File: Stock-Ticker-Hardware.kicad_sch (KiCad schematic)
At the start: 0 parts

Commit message: Start schematic
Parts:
- added A1: RaspberryPi_Pico_W, Module:RaspberryPi_Pico_W_SMD_HandSolder, symbol MCU_Module:RaspberryPi_Pico_W_Debug
- added J1: Conn_01x05_Socket, Connector_JST:JST_XH_B5B-XH-A_1x05_P2.50mm_Vertical, symbol Connector:Conn_01x05_Socket
- added SW1: SW_Push, Button_Switch_THT:SW_PUSH-12mm, symbol Switch:SW_Push
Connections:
- new net: A1.22 (GPIO17), SW1.1
- new net +5V: A1.40 (VBUS), J1.5 (Pin_5)
- new net CLK: A1.4 (GPIO2), J1.1 (Pin_1)
- new net CS: A1.5 (GPIO3), J1.3 (Pin_3)
- new net DOUT: A1.7 (GPIO5), J1.2 (Pin_2)
- new net GND: A1.13 (GND), A1.18 (GND), A1.23 (GND), A1.28 (GND), A1.3 (GND), A1.38 (GND), A1.8 (GND), A1.D2 (GND), J1.4 (Pin_4), SW1.2

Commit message: Finish basic schematic
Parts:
- added H1, H2, H3, H4: MountingHole, MountingHole:MountingHole_2.7mm_M2.5, symbol Mechanical:MountingHole
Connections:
- no-connect marks 0 -> 30
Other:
- title: (none) -> Stock Ticker Hardware
- moved on the sheet: A1, J1, SW1

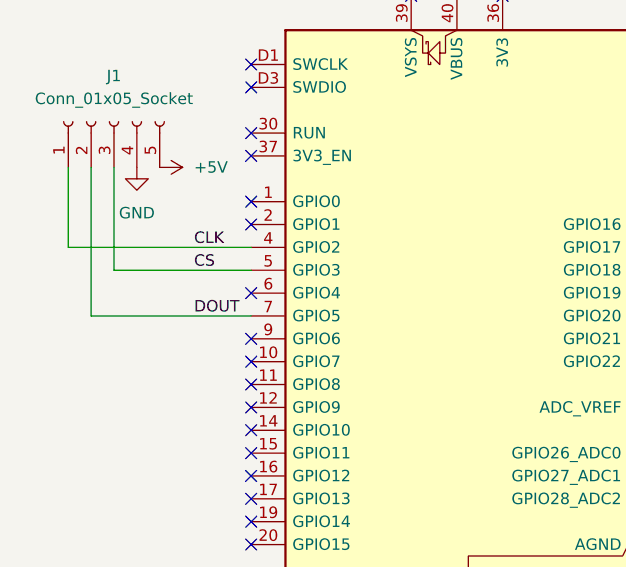
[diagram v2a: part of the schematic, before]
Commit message: Correct wiring from Pico to JST XH
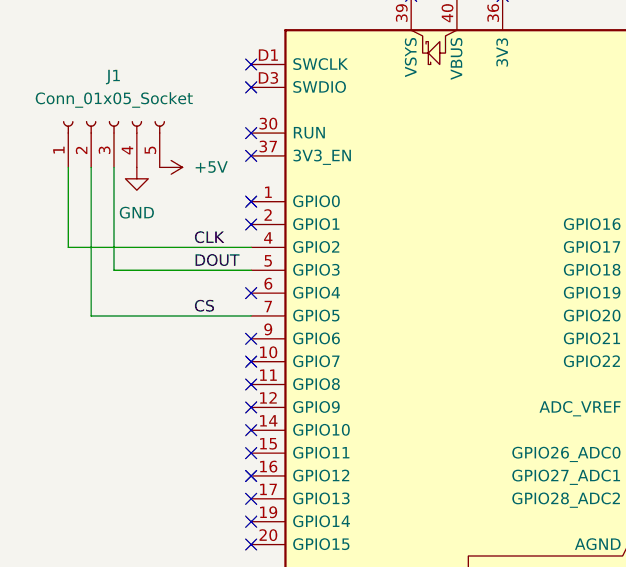
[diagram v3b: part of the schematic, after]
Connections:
- net CS: now also A1.7 (GPIO5), J1.2 (Pin_2); no longer A1.5 (GPIO3), J1.3 (Pin_3)
- net DOUT: now also A1.5 (GPIO3), J1.3 (Pin_3); no longer A1.7 (GPIO5), J1.2 (Pin_2)
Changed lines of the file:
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@@
+	(wire
+		(pts
+			(xy 99.06 90.17) (xy 114.3 90.17)
+		)
+		(stroke
+			(width 0)
+			(type default)
+		)
+	)
 	(wire
 		(pts
 			(xy 99.06 78.74) (xy 99.06 90.17)
+		)
+		(stroke
+			(width 0)
+			(type default)
+		)
+	)
+	(wire
+		(pts
+			(xy 96.52 95.25) (xy 114.3 95.25)
 		)
 		(stroke
@@
 		)
 	)
-	(wire
-		(pts
-			(xy 99.06 90.17) (xy 114.3 90.17)
-		)
-		(stroke
-			(width 0)
-			(type default)
-		)
-	)
-	(wire
-		(pts
-			(xy 96.52 95.25) (xy 114.3 95.25)
-		)
-		(stroke
-			(width 0)
-			(type default)
-		)
-	)
 	(label "CLK"
 		(at 107.95 87.63 0)
@@
 	)
 	(label "CS"
-		(at 107.95 90.17 0)
+		(at 107.95 95.25 0)
 		(effects
 			(font
@@
 	)
 	(label "DOUT"
-		(at 107.95 95.25 0)
+		(at 107.95 90.17 0)
 		(effects
 			(font

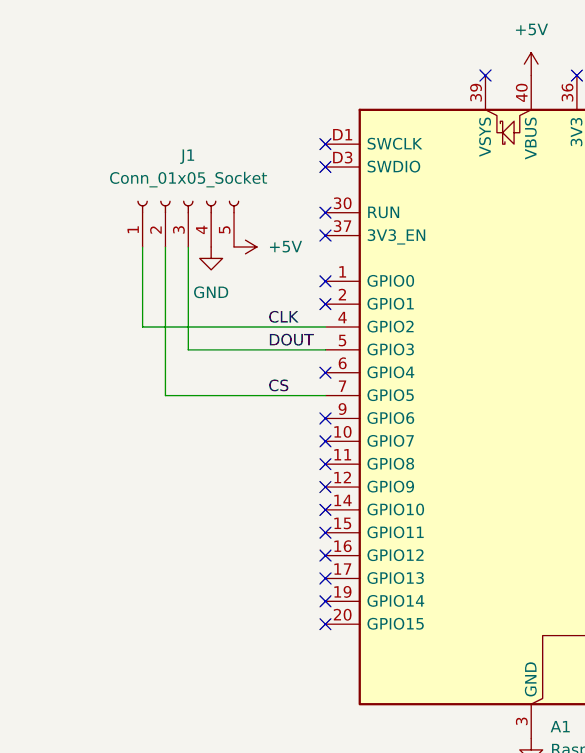
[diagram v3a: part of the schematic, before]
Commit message: Add connectors for SWD and UART for easy debugging
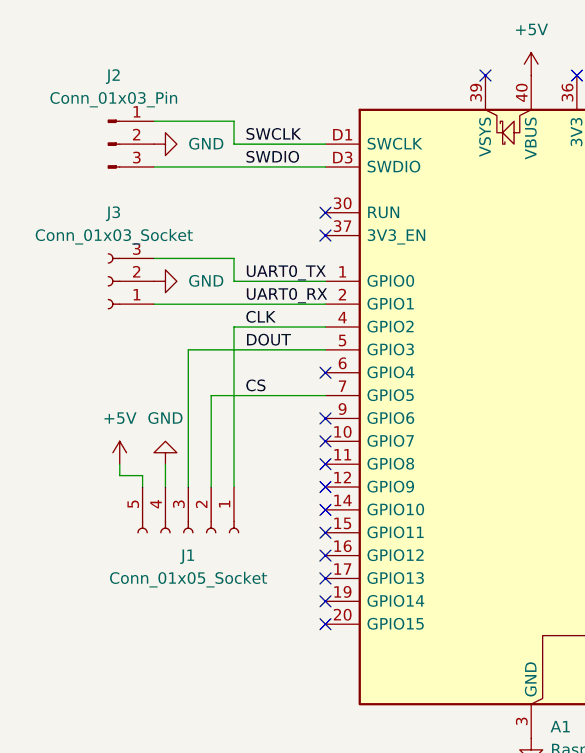
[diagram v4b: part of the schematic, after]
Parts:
- added J2: Conn_01x03_Pin, Connector_PinHeader_2.54mm:PinHeader_1x03_P2.54mm_Vertical, symbol Connector:Conn_01x03_Pin
- added J3: Conn_01x03_Socket, Connector_PinSocket_2.54mm:PinSocket_1x03_P2.54mm_Vertical, symbol Connector:Conn_01x03_Socket
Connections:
- net GND: now also J2.2 (Pin_2), J3.2 (Pin_2)
- net UART0_TX: now reaches A1.1 (GPIO0)
- net UART0_TX: now also J3.3 (Pin_3)
- net UART0_RX: now reaches A1.2 (GPIO1)
- net UART0_RX: now also J3.1 (Pin_1)
- net SWCLK: now reaches A1.D1 (SWCLK)
- net SWCLK: now also J2.1 (Pin_1)
- net SWDIO: now reaches A1.D3 (SWDIO)
- net SWDIO: now also J2.3 (Pin_3)
- no-connect marks 30 -> 26
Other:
- moved on the sheet: J1

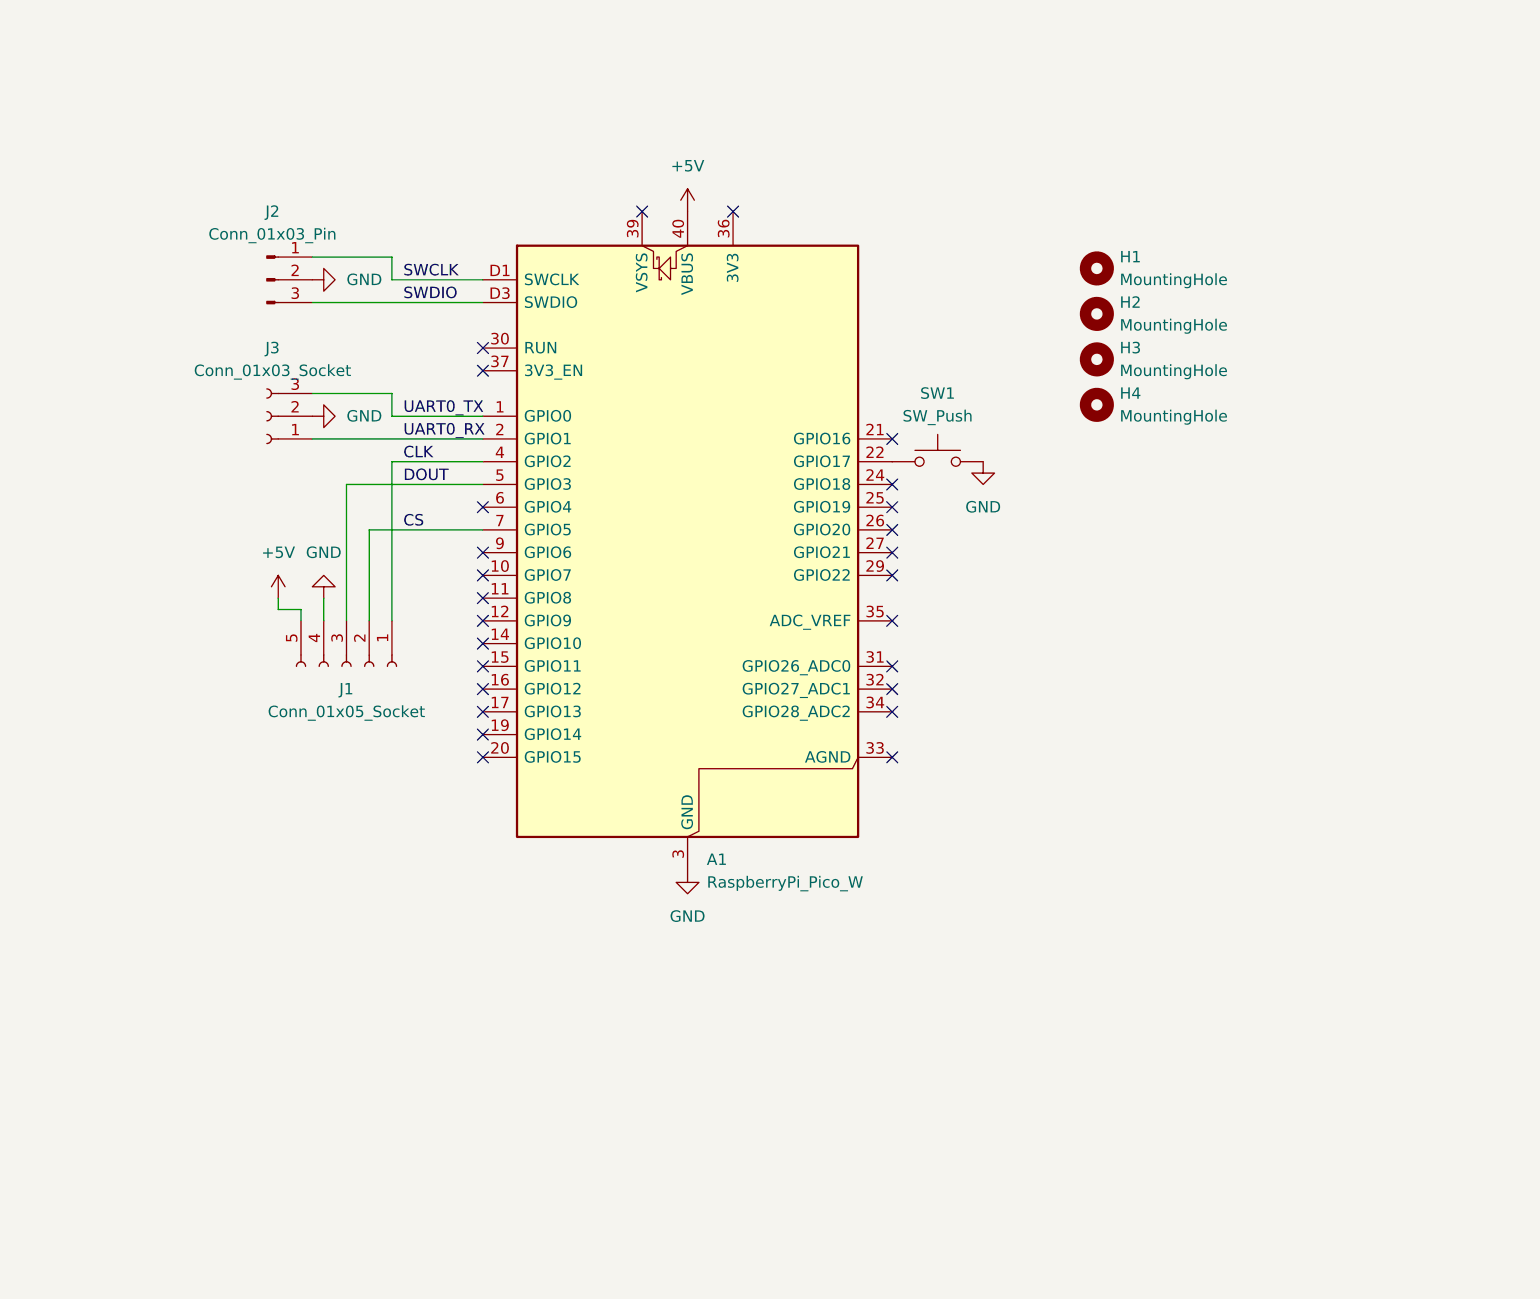
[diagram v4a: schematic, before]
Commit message: Better schematic with level shifter, decoup caps, delete PCB
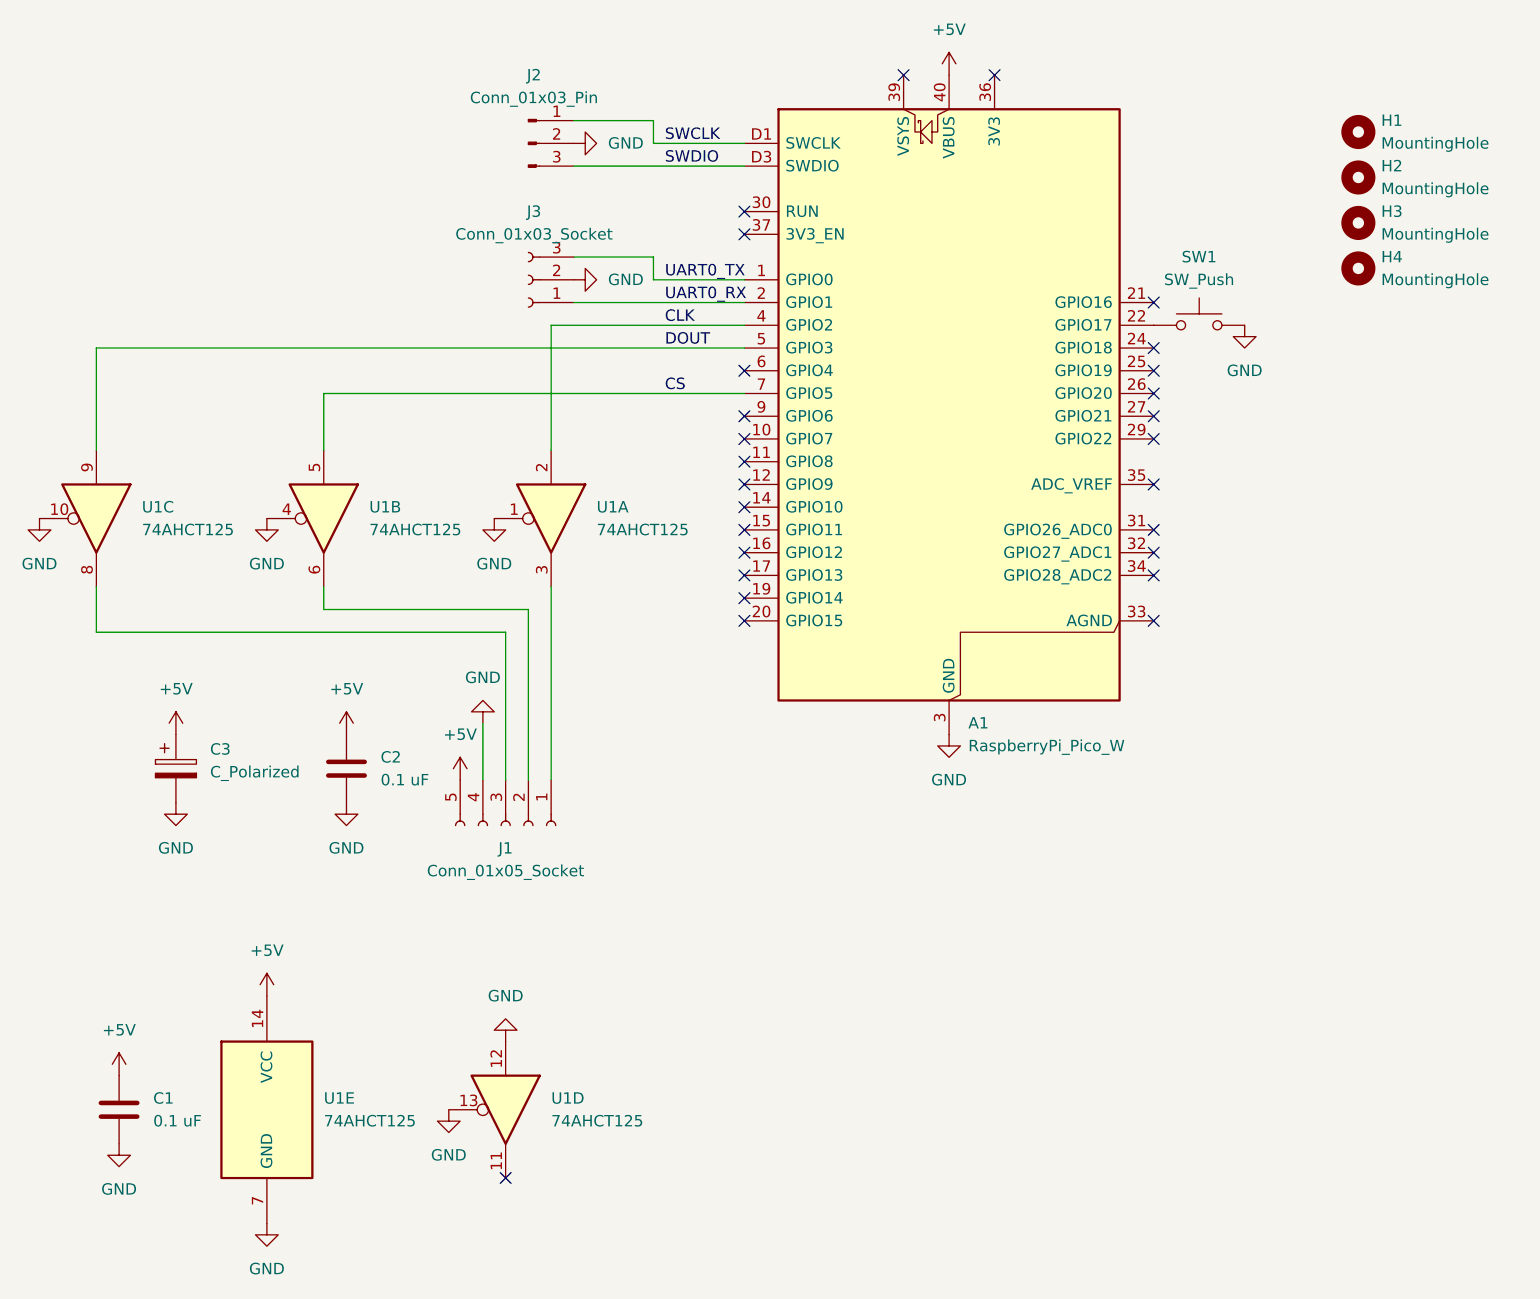
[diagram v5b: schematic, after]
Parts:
- added C1, C2: 0.1 uF, Capacitor_THT:C_Disc_D5.0mm_W2.5mm_P2.50mm, symbol Device:C
- added C3: C_Polarized, Capacitor_THT:CP_Radial_D4.0mm_P2.00mm, symbol Device:C_Polarized
- added U1: 74AHCT125, Package_DIP:DIP-14_W7.62mm, symbol 74xx:74AHCT125
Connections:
- net +5V: now also C1.1, C2.1, C3.1, U1.14 (VCC)
- net CLK: now also U1.2; no longer J1.1 (Pin_1)
- net CS: now also U1.5; no longer J1.2 (Pin_2)
- net DOUT: now also U1.9; no longer J1.3 (Pin_3)
- net GND: now also C1.2, C2.2, C3.2, U1.1, U1.10, U1.12, U1.13, U1.4, U1.7 (GND)
- new net: J1.2 (Pin_2), U1.6
- new net: J1.1 (Pin_1), U1.3
- new net: J1.3 (Pin_3), U1.8
- no-connect marks 26 -> 27
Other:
- moved on the sheet: A1, H1, H2, H3, H4, J1, J2, J3, SW1

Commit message: Finish routing
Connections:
- net at A1.22 (GPIO17): no longer SW1.1
- net at A1.29 (GPIO22): now also SW1.1
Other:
- moved on the sheet: SW1
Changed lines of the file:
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@@
+	)
+	(no_connect
+		(at 189.23 72.39)
 	)
 	(no_connect
@@
 	(no_connect
 		(at 189.23 100.33)
-	)
-	(no_connect
-		(at 189.23 85.09)
 	)
 	(no_connect
@@
 	(symbol
 		(lib_id "Switch:SW_Push")
-		(at 194.31 72.39 0)
+		(at 194.31 85.09 0)
 		(unit 1)
 		(exclude_from_sim no)
@@
 		(fields_autoplaced yes)
 		(property "Reference" "SW1"
-			(at 194.31 64.77 0)
+			(at 194.31 77.47 0)
 			(effects
 				(font
@@
 		)
 		(property "Value" "SW_Push"
-			(at 194.31 67.31 0)
+			(at 194.31 80.01 0)
 			(effects
 				(font
@@
 		)
 		(property "Footprint" "Button_Switch_THT:SW_PUSH-12mm"
-			(at 194.31 67.31 0)
+			(at 194.31 80.01 0)
 			(effects
 				(font
@@
 		)
 		(property "Datasheet" "~"
-			(at 194.31 67.31 0)
+			(at 194.31 80.01 0)
 			(effects
 				(font
@@
 		)
 		(property "Description" "Push button switch, generic, two pins"
-			(at 194.31 72.39 0)
+			(at 194.31 85.09 0)
 			(effects
 				(font
@@
 		)
 		(instances
-			(project ""
+			(project "Stock-Ticker-Hardware"
 				(path "/e63e39d7-6ac0-4ffd-8aa3-1841a4541b55"
 					(reference "SW1")
@@
 	(symbol
 		(lib_id "power:GND")
-		(at 199.39 72.39 0)
+		(at 199.39 85.09 0)
 		(unit 1)
 		(exclude_from_sim no)
@@
 		(fields_autoplaced yes)
 		(property "Reference" "#PWR03"
-			(at 199.39 78.74 0)
+			(at 199.39 91.44 0)
 			(effects
 				(font
@@
 		)
 		(property "Value" "GND"
-			(at 199.39 77.47 0)
+			(at 199.39 90.17 0)
 			(effects
 				(font
@@
 		)
 		(property "Footprint" ""
-			(at 199.39 72.39 0)
+			(at 199.39 85.09 0)
 			(effects
 				(font
@@
 		)
 		(property "Datasheet" ""
-			(at 199.39 72.39 0)
+			(at 199.39 85.09 0)
 			(effects
 				(font
@@
 		)
 		(property "Description" "Power symbol creates a global label with name \"GND\" , ground"
-			(at 199.39 72.39 0)
-			(effects
-				(font
-					(size 1.27 1.27)
-				)
-				(hide yes)
-			)
-		)
-		(pin "1"
-		)
-		(instances
-			(project ""
+			(at 199.39 85.09 0)
+			(effects
+				(font
+					(size 1.27 1.27)
+				)
+				(hide yes)
+			)
+		)
+		(pin "1"
+		)
+		(instances
+			(project "Stock-Ticker-Hardware"
 				(path "/e63e39d7-6ac0-4ffd-8aa3-1841a4541b55"
 					(reference "#PWR03")

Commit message: Finish actual routing this time
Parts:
- added C4: 0.1 μF, Capacitor_THT:C_Disc_D5.0mm_W2.5mm_P2.50mm, symbol Device:C
- added R1: 10 kΩ, Resistor_THT:R_Axial_DIN0207_L6.3mm_D2.5mm_P10.16mm_Horizontal, symbol Device:R_US
- added R2: 1 kΩ, Resistor_THT:R_Axial_DIN0207_L6.3mm_D2.5mm_P10.16mm_Horizontal, symbol Device:R_US
- C1, C2: value 0.1 uF -> 0.1 μF
- C3: value C_Polarized -> 10 μF
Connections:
- net GND: now also C4.2
- net at A1.29 (GPIO22): now also R2.1; no longer SW1.1
- net +3.3V: now reaches A1.36 (3V3)
- net +3.3V: now also R1.1
- new net: C4.1, R1.2, R2.2, SW1.1
- no-connect marks 27 -> 26
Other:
- moved on the sheet: C3, SW1
